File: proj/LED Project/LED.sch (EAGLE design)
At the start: 14 parts, among them J2 AVR_SPI_PROG_3X2PTH, J3 POWER_JACKPTH_BREAD, J4 6_PIN_SERIAL_CABLEPTH, U1 328P

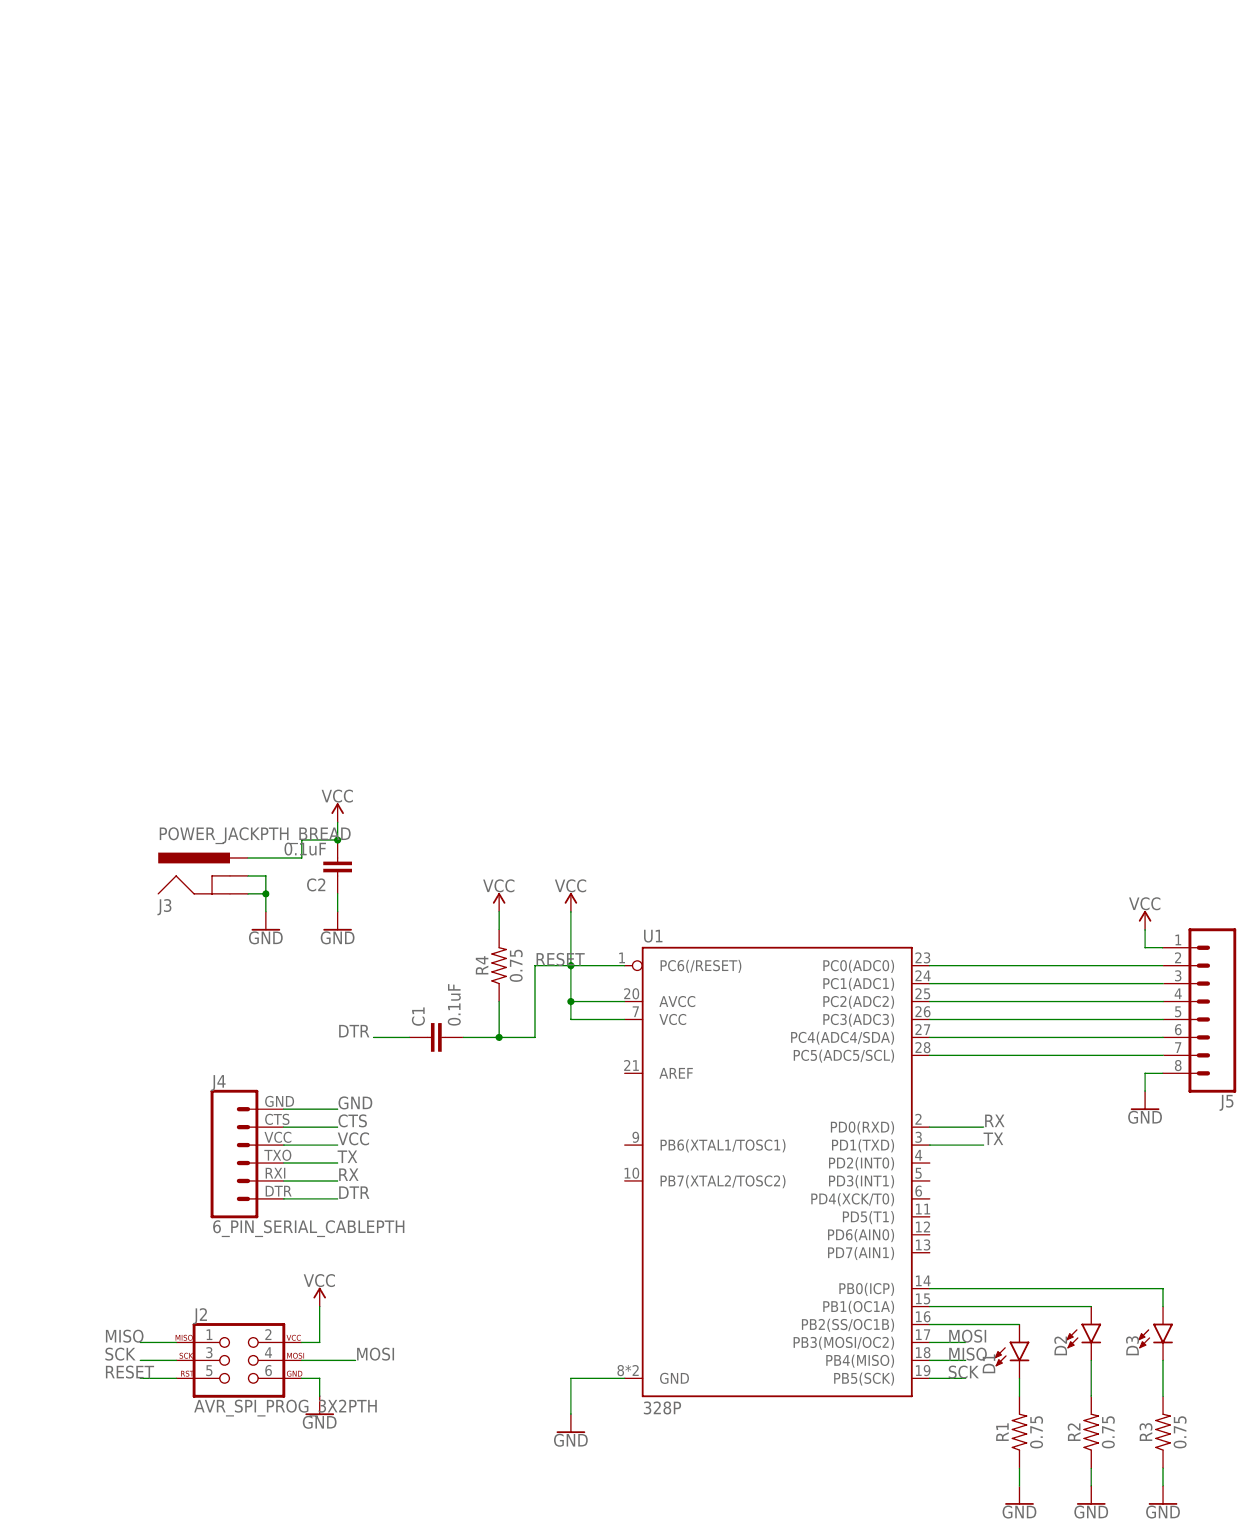
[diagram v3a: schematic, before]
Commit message: Fixing Board Errors
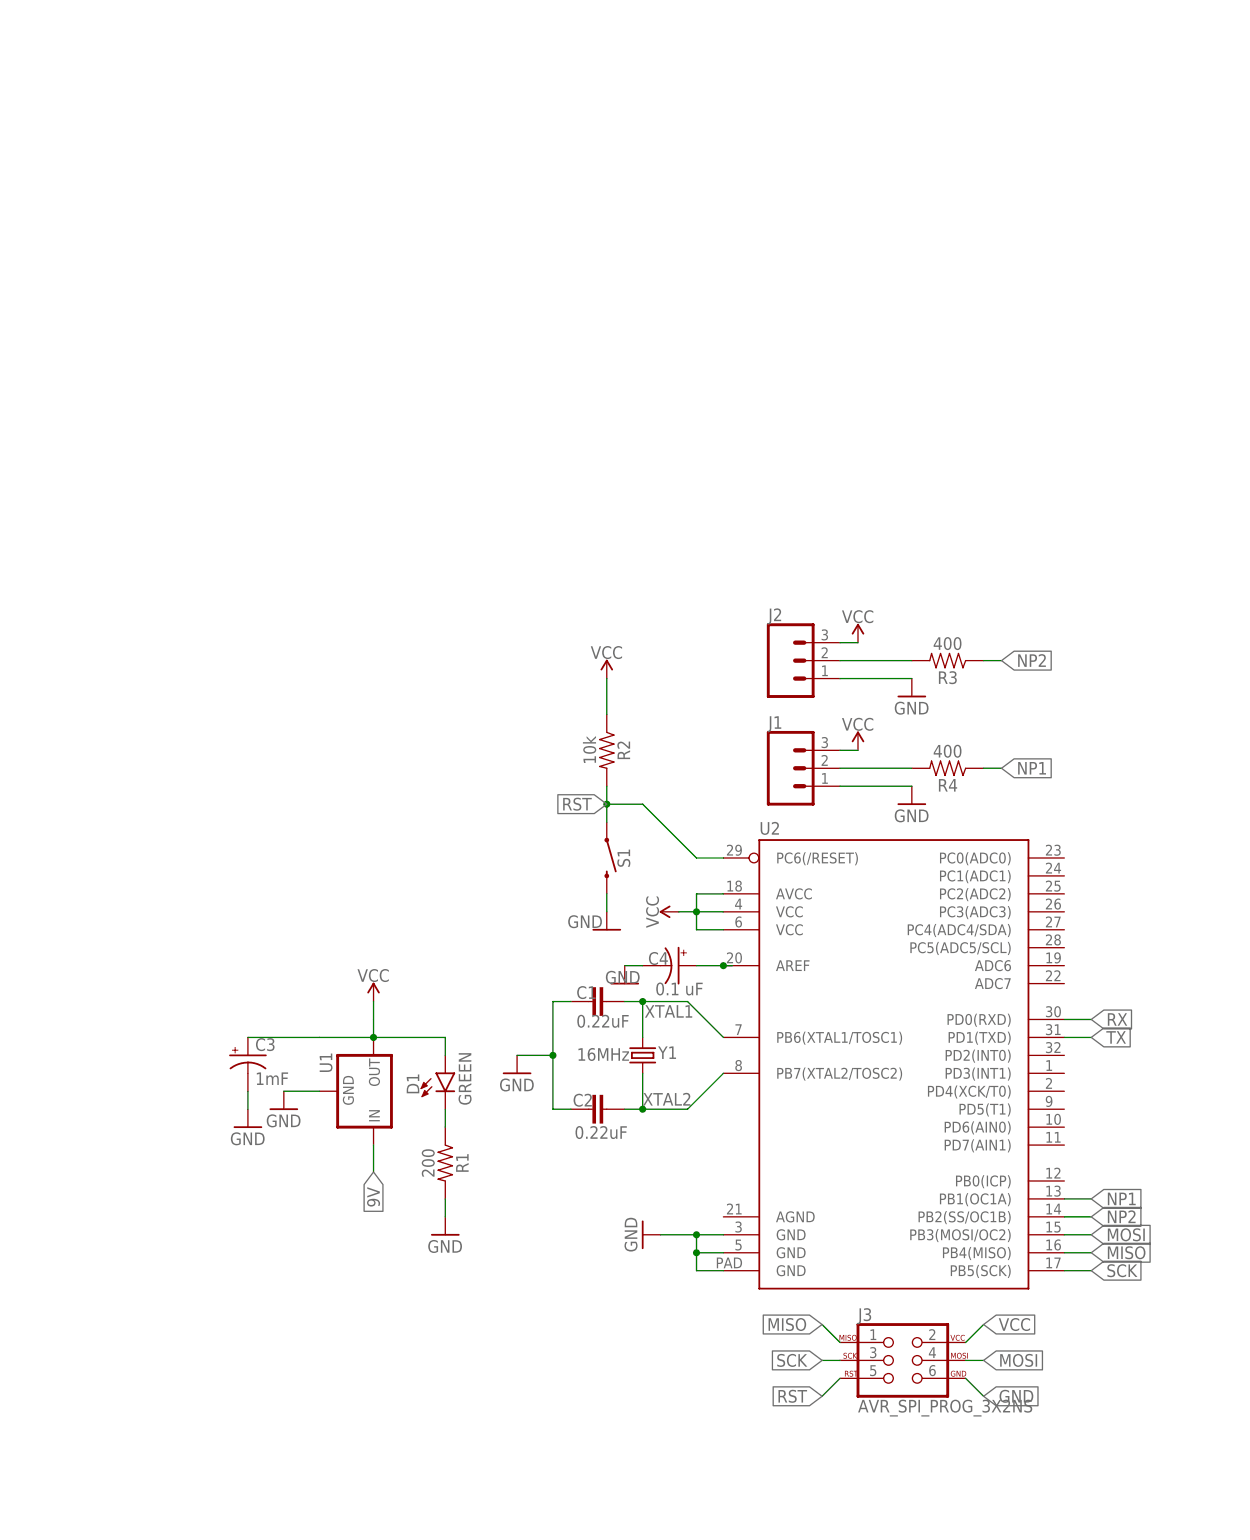
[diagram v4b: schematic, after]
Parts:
- removed D2, D3: (no value), SparkFun-LED:LED5MM
- removed J4: 6_PIN_SERIAL_CABLEPTH, SparkFun-Connectors:6_PIN_SERIAL_CABLEPTH
- removed J5: (no value), SparkFun-Connectors:CONN_08"
- added C3: 1mF, SparkFun-Capacitors:1000UF-RADIAL-5MM-25V-20%
- added C4: 0.1 uF, SparkFun-Capacitors:1000UF-RADIAL-5MM-25V-20%
- added J1: (no value), SparkFun-Connectors:CONN_03
- added S1: MOMENTARY-SWITCH-SPST-PTH-6.0MM-KIT, SparkFun-Switches:MOMENTARY-SWITCH-SPST-PTH-6.0MM-KIT
- added U2: (no value), SparkFun-IC-Microcontroller:ATMEGA328P_MLFMLF32
- added Y1: 16MHz, SparkFun-Clocks:CRYSTAL-16MHZPTH-HC49US
- C1, C2: value 0.1uF -> 0.22uF; device SparkFun-Capacitors:0.1UF-0402-16V-10% -> SparkFun-Capacitors:0.22UF-0603-25V-10%
- D1: value (none) -> GREEN; device SparkFun-LED:LED5MM -> SparkFun-LED:LED-GREEN0603
- J2: value AVR_SPI_PROG_3X2PTH -> (none); device SparkFun-Connectors:AVR_SPI_PROG_3X2PTH -> SparkFun-Connectors:CONN_03
- J3: value POWER_JACKPTH_BREAD -> AVR_SPI_PROG_3X2NS; device SparkFun-Connectors:POWER_JACKPTH_BREAD -> SparkFun-Connectors:AVR_SPI_PROG_3X2NS
- R1: value 0.75 -> 200; device SparkFun-Resistors:0.75OHM-0805-1/4W-1% -> SparkFun-Resistors:470OHM-0603-1/10W-1%
- R2: value 0.75 -> 10k; device SparkFun-Resistors:0.75OHM-0805-1/4W-1% -> SparkFun-Resistors:470OHM-0603-1/10W-1%
- R3, R4: value 0.75 -> 400; device SparkFun-Resistors:0.75OHM-0805-1/4W-1% -> SparkFun-Resistors:470OHM-0603-1/10W-1%
- U1: value 328P -> R-78E5.0-1.0; device SparkFun-IC-Microcontroller:ATMEGA328P_PDIP -> SparkFun-IC-Power:R-78E5.0-1.0
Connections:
- removed net CTS: J4.5
- removed net DTR: C1.1, J4.1
- removed net N$1: J5.2, U1.PC0(ADC0)
- removed net N$11: D2.A, U1.PB1(OC1A)
- removed net N$12: D2.C, R2.2
- removed net N$2: D3.C, R3.2
- removed net N$3: J5.3, U1.PC1(ADC1)
- removed net N$4: J5.4, U1.PC2(ADC2)
- removed net N$5: J5.5, U1.PC3(ADC3)
- removed net N$6: J5.7, U1.PC5(ADC5/SCL)
- removed net N$7: J5.6, U1.PC4(ADC4/SDA)
- removed net N$8: D1.A, U1.PB2(SS/OC1B)
- removed net N$9: D1.C, R1.2
- removed net RESET: C1.2, J2.5, R4.1, U1.AVCC, U1.PC6(/RESET), U1.VCC
- new net 9V: U1.IN
- new net DATA1: J1.2, R4.2
- new net DATA2: J2.2, R3.2
- new net NP1: R4.1, U2.PB1(OC1A)
- new net NP2: R3.1, U2.PB2(SS/OC1B)
- new net RST: J3.5, R2.2, S1.1, U2.PC6(/RESET)
- new net VCC1: C4.+, U2.AREF
- new net XTAL1: C1.1, U2.PB6(XTAL1/TOSC1), Y1.1
- new net XTAL2: C2.1, U2.PB7(XTAL2/TOSC2), Y1.2
- net GND: now also C1.2, C2.2, C3.-, C4.-, J1.1, J2.1, J3.6, R1.2, S1.2, U2.GND@3, U2.GND@5, U2.GND@PAD; no longer C2.1, J2.6, J3.GND, J3.GNDBREAK, J4.6, J5.8, R1.1, R2.1, R3.1
- net MISO: now also J3.1, U2.PB4(MISO); no longer J2.1, U1.PB4(MISO)
- net MOSI: now also J3.4, U2.PB3(MOSI/OC2); no longer J2.4, U1.PB3(MOSI/OC2)
- net N$10: now also D1.C, R1.1; no longer D3.A, U1.PB0(ICP)
- net RX: now also U2.PD0(RXD); no longer J4.2, U1.PD0(RXD)
- net SCK: now also J3.3, U2.PB5(SCK); no longer J2.3, U1.PB5(SCK)
- net TX: now also U2.PD1(TXD); no longer J4.3, U1.PD1(TXD)
- net VCC: now also C3.+, D1.A, J1.3, J2.3, J3.2, R2.1, U1.OUT, U2.AVCC, U2.VCC@4, U2.VCC@6; no longer C2.2, J2.2, J3.PWR, J4.4, J5.1, R4.2
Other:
- moved on the sheet: C1, C2, D1, R1, R2, R3, R4

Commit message: fixing schematic
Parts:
- added C5: 10uF, SparkFun-Capacitors:1000UF-RADIAL-5MM-25V-20%
- added C6: 10uF, rcl:C-USC0805
- U2: value (none) -> ATMEGA328P_MLF
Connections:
- net VCC1 renamed N$1
- new net N$2: C3.+
- new net N$5: C6.1, U1.OUT
- net 9V: now also C5.+
- net GND: now also C5.-, C6.2, U2.AGND
- net VCC: no longer C3.+, U1.OUT
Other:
- moved on the sheet: C3, D1, R1, U1

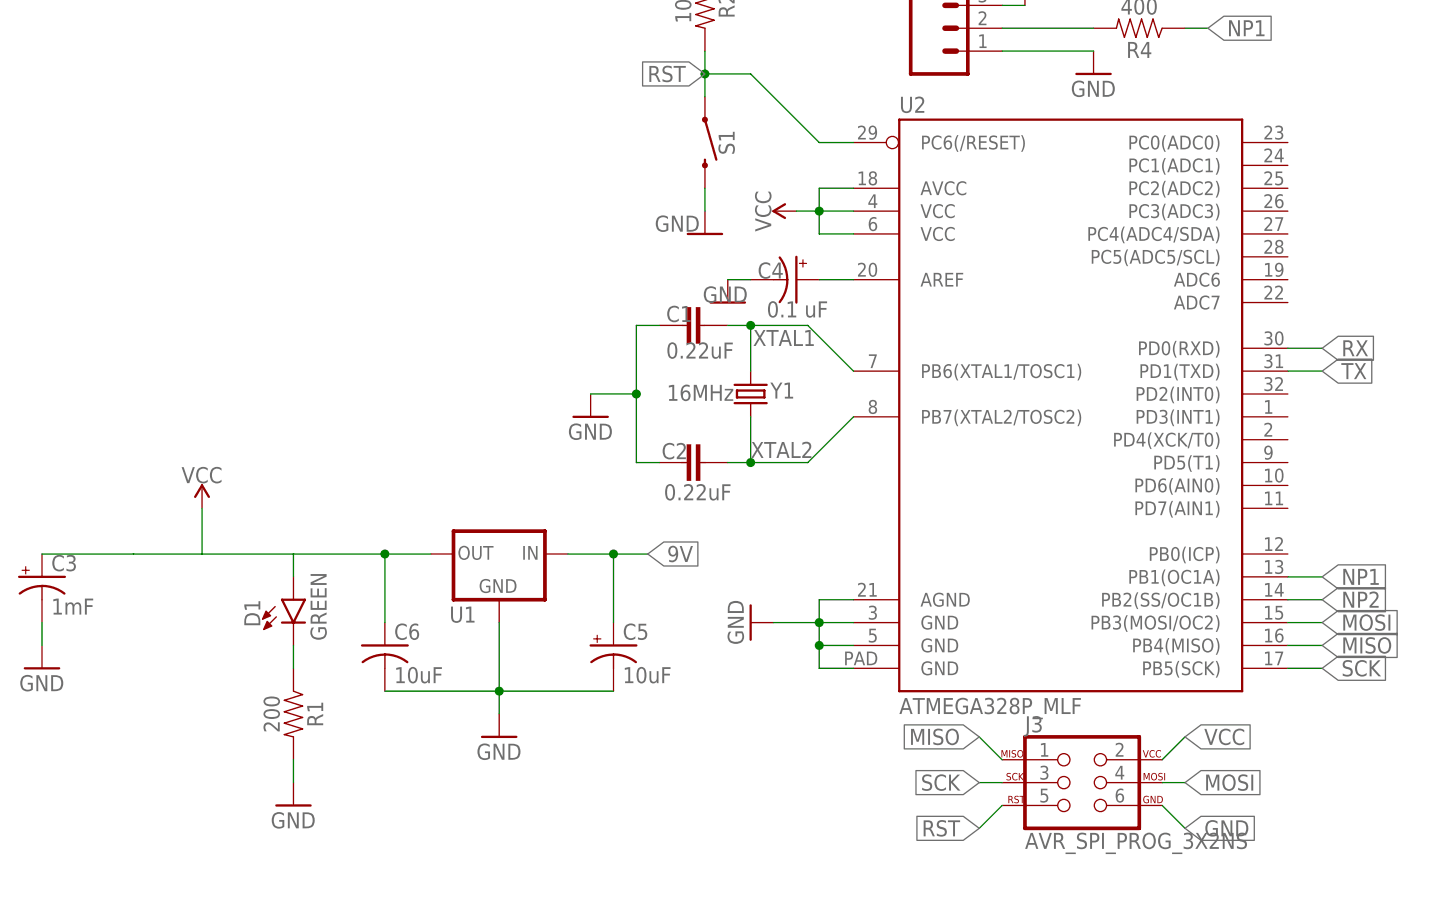
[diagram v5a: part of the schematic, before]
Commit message: Added IGVC lbr so I have them and a fuse
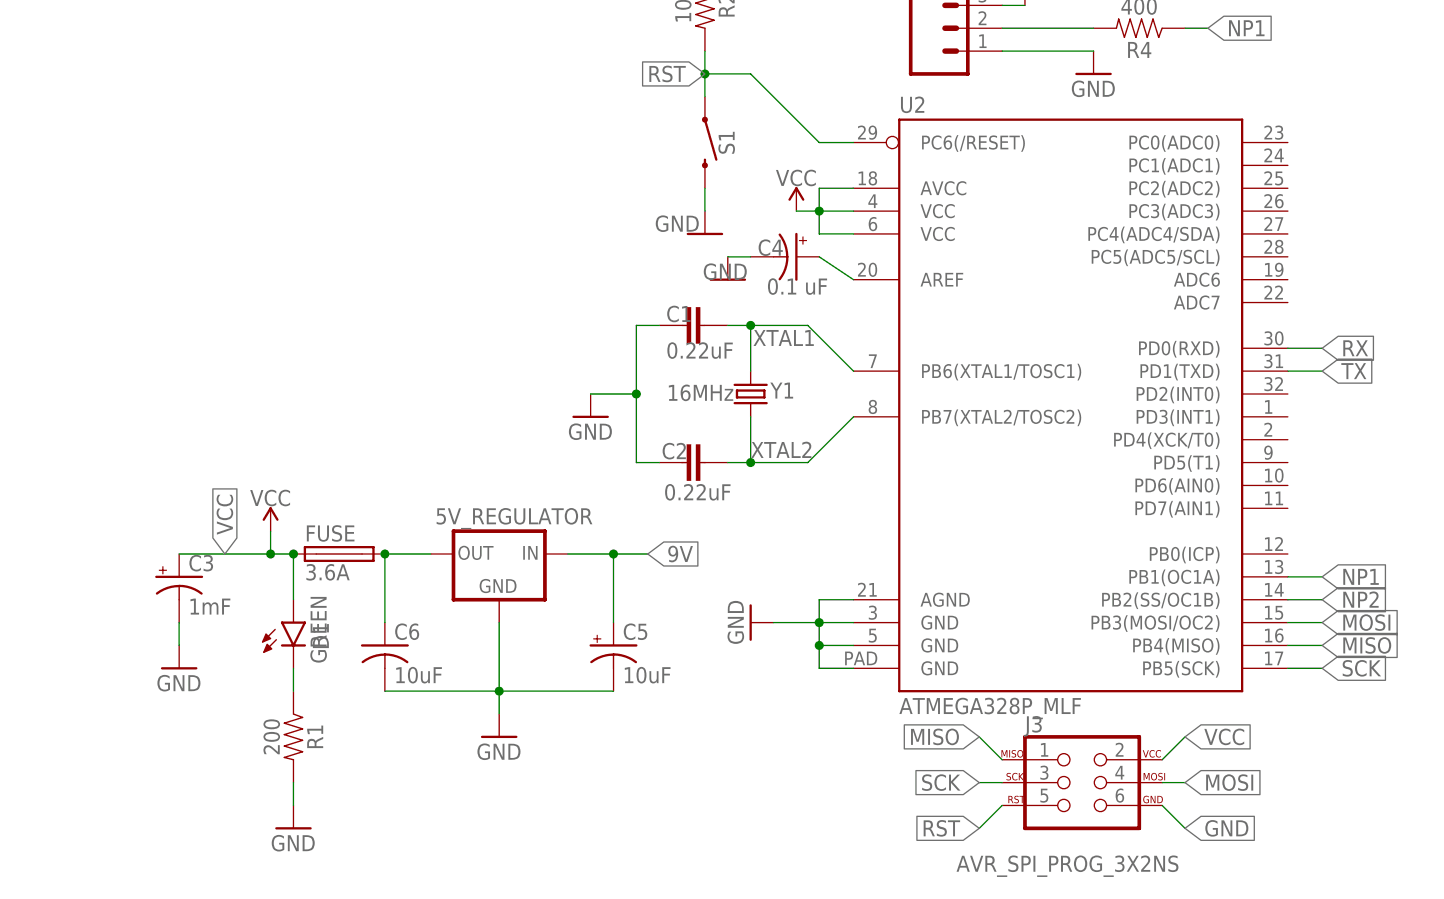
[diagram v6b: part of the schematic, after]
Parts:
- added FUSE: 3.6A, IGVC-Misc:FUSE_HOLDER
- J2: SPICEPREFIX (none) -> J
- renumbered U1 to 5V_REGULATOR
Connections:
- removed net N$2: C3.+
- net N$5: now also FUSE.2
- net VCC: now also C3.+, FUSE.1
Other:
- moved on the sheet: C3, C4, D1, R1
